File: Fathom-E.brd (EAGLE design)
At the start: 38.1 x 45.7 mm, 6 parts

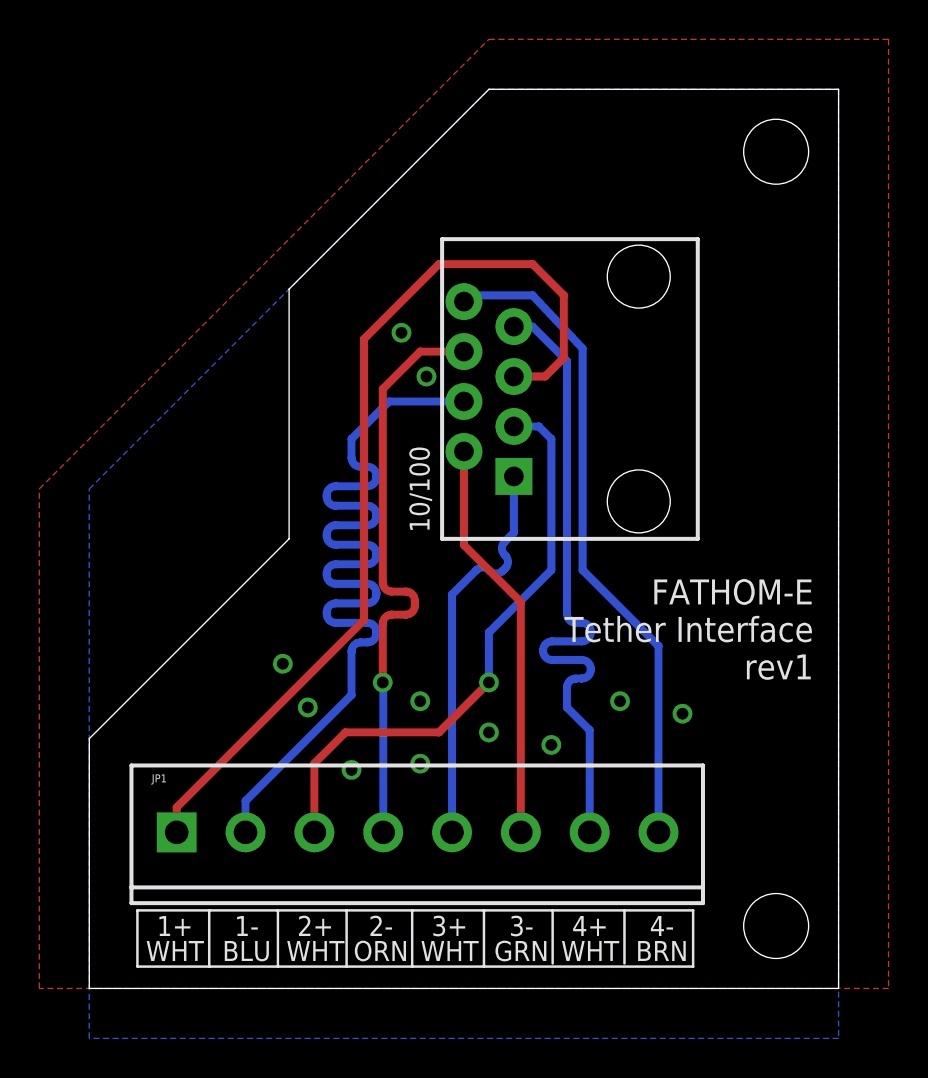
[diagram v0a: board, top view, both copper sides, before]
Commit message: Updated RJ45 position on Fathom-E
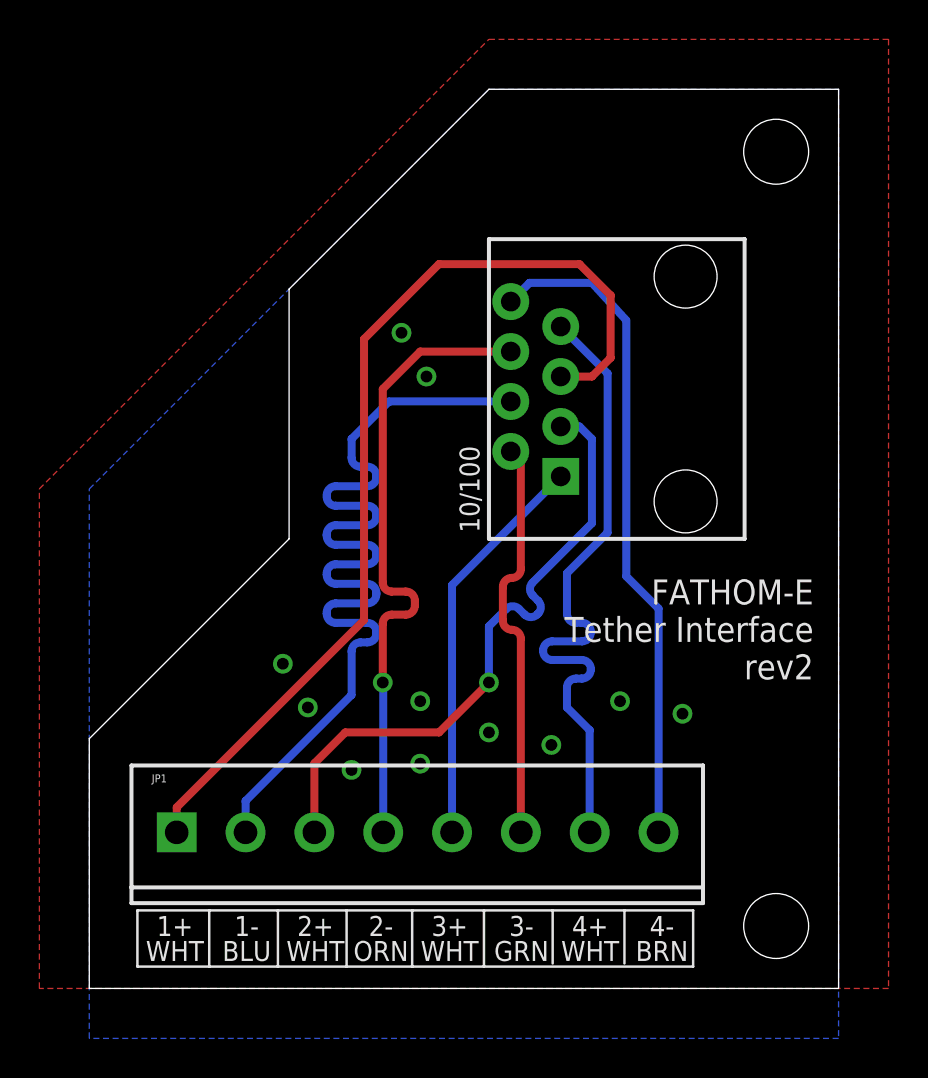
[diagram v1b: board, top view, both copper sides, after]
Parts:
- U$1: value RJ45-8PTH -> RJ45-8PTH-H; device SparkFun-Connectors:RJ45-8 -> BlueRobotics-Main:RJ45-8
- moved U$1 2.38 mm to (30.3, 30.5)
- moved U$7 1.27 mm to (30.8, 7.30)
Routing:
- net ORANGE: track 29.7 -> 32.0 mm
- net BLUE-WHITE: track 47.5 -> 49.9 mm
- net BLUE: track 46.1 -> 48.5 mm
- net ORANGE-WHITE: track 30.0 -> 32.0 mm
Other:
- board text added: "FATHOM-E Tether Interface rev2"
- board text added: "R.J. 2016/05"
- board text removed: "FATHOM-E Tether Interface rev1"
- board text removed: "R.J. 2016/02"
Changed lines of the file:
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@@
 <text x="36.83" y="18.25625" size="1.27" layer="21" ratio="12" align="center-right">FATHOM-E
 Tether Interface
-rev1</text>
+rev2</text>
 <wire x1="30.705" y1="3.96875" x2="27.2125" y2="3.96875" width="0.127" layer="21"/>
 <wire x1="27.2125" y1="3.96875" x2="23.56125" y2="3.96875" width="0.127" layer="21"/>
@@
 WHT</text>
 <text x="30.48" y="1.27" size="1.016" layer="22" rot="MR0">For cable lengths of 100m or less</text>
-<text x="10.16" y="19.84375" size="1.016" layer="22" ratio="12" rot="MR315">R.J. 2016/02</text>
-<text x="17.30375" y="23.1775" size="1.016" layer="21" ratio="12" rot="R90">10/100</text>
+<text x="10.16" y="19.84375" size="1.016" layer="22" ratio="12" rot="MR315">R.J. 2016/05</text>
+<text x="19.84375" y="23.1775" size="1.016" layer="21" ratio="12" rot="R90">10/100</text>
 </plain>
 <attributes>
@@
 <element name="STANDOFF3" library="SparkFun-Electromechanical" package="STAND-OFF" value="STAND-OFF" x="34.925" y="42.545"/>
 <element name="U$6" library="BlueRobotics-Main" package="BR-LOGO-MEDIUM-SMALL-COPPER" value="LOGOBR-LOGO-MS-COPPER" x="20.0025" y="39.37"/>
-<element name="U$7" library="BlueRobotics-Main" package="BR-FULL-LOGO-MEDIUM" value="LOGOFULL-M" x="29.5275" y="7.3025" rot="MR90"/>
-<element name="U$1" library="SparkFun-Connectors" package="RJ45-8" value="RJ45-8PTH" x="27.94" y="30.48" rot="R90"/>
+<element name="U$7" library="BlueRobotics-Main" package="BR-FULL-LOGO-MEDIUM" value="LOGOFULL-M" x="30.7975" y="7.3025" rot="MR90"/>
+<element name="U$1" library="BlueRobotics-Main" package="RJ45-8" value="RJ45-8PTH-H" x="30.32125" y="30.48" rot="R90"/>
 <element name="JP1" library="SparkFun-Connectors" package="SCREWTERMINAL-3.5MM-8" value="" x="4.445" y="7.9375"/>
 </elements>
@@
 <contactref element="U$1" pad="8"/>
 <contactref element="JP1" pad="8"/>
-<wire x1="28.945" y1="7.9375" x2="28.945" y2="17.41" width="0.4064" layer="16"/>
-<wire x1="28.945" y1="17.41" x2="25.0825" y2="21.2725" width="0.4064" layer="16"/>
-<wire x1="25.0825" y1="21.2725" x2="25.0825" y2="32.54375" width="0.4064" layer="16"/>
-<wire x1="25.0825" y1="32.54375" x2="22.5425" y2="35.2425" width="0.4064" layer="16"/>
-<wire x1="22.5425" y1="35.2425" x2="19.3675" y2="35.2425" width="0.4064" layer="16"/>
-<wire x1="19.3675" y1="35.2425" x2="19.05" y2="34.925" width="0.4064" layer="16"/>
+<wire x1="28.945" y1="7.9375" x2="28.945" y2="19.315" width="0.4064" layer="16"/>
+<wire x1="28.945" y1="19.315" x2="27.305" y2="20.955" width="0.4064" layer="16"/>
+<wire x1="27.305" y1="20.955" x2="27.305" y2="33.9725" width="0.4064" layer="16"/>
+<wire x1="27.305" y1="33.9725" x2="25.55875" y2="35.8775" width="0.4064" layer="16"/>
+<wire x1="25.55875" y1="35.8775" x2="22.38375" y2="35.8775" width="0.4064" layer="16"/>
+<wire x1="22.38375" y1="35.8775" x2="21.43125" y2="34.925" width="0.4064" layer="16"/>
 </signal>
 <signal name="BROWN-WHITE">
@@
 <wire x1="25.04365" y1="18.5928" x2="24.74595" y2="18.5928" width="0.4064" layer="16"/>
 <wire x1="24.74595" y1="18.5928" x2="24.28875" y2="19.05" width="0.4064" layer="16" curve="-90"/>
-<wire x1="24.28875" y1="19.05" x2="24.28875" y2="31.90875" width="0.4064" layer="16"/>
-<wire x1="24.28875" y1="31.90875" x2="22.5425" y2="33.655" width="0.4064" layer="16"/>
-<wire x1="22.5425" y1="33.655" x2="21.59" y2="33.655" width="0.4064" layer="16"/>
+<wire x1="24.28875" y1="19.05" x2="24.28875" y2="21.11375" width="0.4064" layer="16"/>
+<wire x1="24.28875" y1="21.11375" x2="26.3525" y2="23.1775" width="0.4064" layer="16"/>
+<wire x1="26.3525" y1="23.1775" x2="26.3525" y2="31.27375" width="0.4064" layer="16"/>
+<wire x1="26.3525" y1="31.27375" x2="23.97125" y2="33.655" width="0.4064" layer="16"/>
 </signal>
 <signal name="ORANGE">
@@
 <contactref element="JP1" pad="4"/>
 <wire x1="14.9225" y1="30.48" x2="16.8275" y2="32.385" width="0.4064" layer="1"/>
-<wire x1="16.8275" y1="32.385" x2="19.05" y2="32.385" width="0.4064" layer="1"/>
+<wire x1="16.8275" y1="32.385" x2="21.43125" y2="32.385" width="0.4064" layer="1"/>
 <wire x1="14.945" y1="7.9375" x2="14.945" y2="15.535" width="0.4064" layer="16"/>
 <wire x1="14.945" y1="15.535" x2="14.9225" y2="15.5575" width="0.4064" layer="16"/>
@@
 <wire x1="13.97" y1="18.7325" x2="13.97" y2="33.02" width="0.4064" layer="1"/>
 <wire x1="13.97" y1="33.02" x2="17.78" y2="36.83" width="0.4064" layer="1"/>
-<wire x1="17.78" y1="36.83" x2="22.5425" y2="36.83" width="0.4064" layer="1"/>
-<wire x1="22.5425" y1="36.83" x2="24.13" y2="35.2425" width="0.4064" layer="1"/>
-<wire x1="24.13" y1="35.2425" x2="24.13" y2="32.0675" width="0.4064" layer="1"/>
-<wire x1="24.13" y1="32.0675" x2="23.1775" y2="31.115" width="0.4064" layer="1"/>
-<wire x1="23.1775" y1="31.115" x2="21.59" y2="31.115" width="0.4064" layer="1"/>
+<wire x1="17.78" y1="36.83" x2="24.92375" y2="36.83" width="0.4064" layer="1"/>
+<wire x1="24.92375" y1="36.83" x2="26.51125" y2="35.2425" width="0.4064" layer="1"/>
+<wire x1="26.51125" y1="35.2425" x2="26.51125" y2="32.0675" width="0.4064" layer="1"/>
+<wire x1="26.51125" y1="32.0675" x2="25.55875" y2="31.115" width="0.4064" layer="1"/>
+<wire x1="25.55875" y1="31.115" x2="23.97125" y2="31.115" width="0.4064" layer="1"/>
 </signal>
 <signal name="BLUE">
@@
 <wire x1="13.335" y1="26.9875" x2="13.335" y2="27.94" width="0.4064" layer="16"/>
 <wire x1="13.335" y1="27.94" x2="15.24" y2="29.845" width="0.4064" layer="16"/>
-<wire x1="15.24" y1="29.845" x2="19.05" y2="29.845" width="0.4064" layer="16"/>
+<wire x1="15.24" y1="29.845" x2="21.43125" y2="29.845" width="0.4064" layer="16"/>
 </signal>
 <signal name="ORANGE-WHITE">
@@
 <wire x1="17.78" y1="13.0175" x2="20.32" y2="15.5575" width="0.4064" layer="1"/>
 <via x="20.32" y="15.5575" extent="1-16" drill="0.6"/>
-<wire x1="20.32" y1="15.5575" x2="20.32" y2="18.0975" width="0.4064" layer="16"/>
-<wire x1="20.32" y1="18.0975" x2="23.495" y2="21.2725" width="0.4064" layer="16"/>
-<wire x1="23.495" y1="21.2725" x2="23.495" y2="27.94" width="0.4064" layer="16"/>
-<wire x1="23.495" y1="27.94" x2="22.86" y2="28.575" width="0.4064" layer="16"/>
-<wire x1="22.86" y1="28.575" x2="21.59" y2="28.575" width="0.4064" layer="16"/>
+<wire x1="20.32" y1="15.5575" x2="20.32" y2="18.415" width="0.4064" layer="16"/>
+<wire x1="20.32" y1="18.415" x2="21.202959375" y2="19.297959375" width="0.4064" layer="16"/>
+<wire x1="21.202959375" y1="19.297959375" x2="21.8495375" y2="19.297959375" width="0.4064" layer="16" curve="-90"/>
+<wire x1="21.8495375" y1="19.297959375" x2="22.1313875" y2="19.016109375" width="0.4064" layer="16"/>
+<wire x1="22.1313875" y1="19.016109375" x2="22.777965625" y2="19.016109375" width="0.4064" layer="16" curve="90"/>
+<wire x1="22.777965625" y1="19.016109375" x2="22.82435" y2="19.06249375" width="0.4064" layer="16"/>
+<wire x1="22.82435" y1="19.06249375" x2="22.82435" y2="19.709071875" width="0.4064" layer="16" curve="90"/>
+<wire x1="22.82435" y1="19.709071875" x2="22.5425" y2="19.990921875" width="0.4064" layer="16"/>
+<wire x1="22.5425" y1="19.990921875" x2="22.5425" y2="20.6375" width="0.4064" layer="16" curve="-90"/>
+<wire x1="22.5425" y1="20.6375" x2="25.55875" y2="23.65375" width="0.4064" layer="16"/>
+<wire x1="25.55875" y1="23.65375" x2="25.55875" y2="27.94" width="0.4064" layer="16"/>
+<wire x1="25.55875" y1="27.94" x2="24.92375" y2="28.575" width="0.4064" layer="16"/>
+<wire x1="24.92375" y1="28.575" x2="23.97125" y2="28.575" width="0.4064" layer="16"/>
 </signal>
 <signal name="GREEN">
 <contactref element="U$1" pad="2"/>
 <contactref element="JP1" pad="6"/>
-<wire x1="21.945" y1="7.9375" x2="21.945" y2="19.6475" width="0.4064" layer="1"/>
-<wire x1="21.945" y1="19.6475" x2="19.05" y2="22.5425" width="0.4064" layer="1"/>
-<wire x1="19.05" y1="22.5425" x2="19.05" y2="27.305" width="0.4064" layer="1"/>
+<wire x1="21.945" y1="26.79125" x2="21.945" y2="21.33311875" width="0.4064" layer="1"/>
+<wire x1="21.945" y1="21.33311875" x2="21.4878" y2="20.87591875" width="0.4064" layer="1" curve="-90"/>
+<wire x1="21.4878" y1="20.87591875" x2="21.0306" y2="20.41871875" width="0.4064" layer="1" curve="90"/>
+<wire x1="21.0306" y1="20.41871875" x2="21.0306" y2="18.6944" width="0.4064" layer="1"/>
+<wire x1="21.0306" y1="18.6944" x2="21.4878" y2="18.2372" width="0.4064" layer="1" curve="90"/>
+<wire x1="21.4878" y1="18.2372" x2="21.945" y2="17.78" width="0.4064" layer="1" curve="-90"/>
+<wire x1="21.945" y1="17.78" x2="21.945" y2="7.9375" width="0.4064" layer="1"/>
+<wire x1="21.945" y1="26.79125" x2="21.43125" y2="27.305" width="0.4064" layer="1"/>
 </signal>
 <signal name="GREEN-WHITE">
 <contactref element="U$1" pad="1"/>
 <contactref element="JP1" pad="5"/>
-<wire x1="18.445" y1="7.9375" x2="18.445" y2="20.0325" width="0.4064" layer="16"/>
-<wire x1="21.59" y1="23.1775" x2="21.11381875" y2="22.70131875" width="0.4064" layer="16"/>
-<wire x1="21.11381875" y1="22.70131875" x2="21.11381875" y2="22.054740625" width="0.4064" layer="16" curve="90"/>
-<wire x1="21.11381875" y1="22.054740625" x2="21.156571875" y2="22.0119875" width="0.4064" layer="16"/>
-<wire x1="21.156571875" y1="22.0119875" x2="21.156571875" y2="21.36540625" width="0.4064" layer="16" curve="-90"/>
-<wire x1="21.156571875" y1="21.36540625" x2="21.0209125" y2="21.229746875" width="0.4064" layer="16"/>
-<wire x1="21.0209125" y1="21.229746875" x2="20.37433125" y2="21.229746875" width="0.4064" layer="16" curve="-90"/>
-<wire x1="20.37433125" y1="21.229746875" x2="20.331578125" y2="21.2725" width="0.4064" layer="16"/>
-<wire x1="20.331578125" y1="21.2725" x2="19.685" y2="21.2725" width="0.4064" layer="16" curve="90"/>
-<wire x1="19.685" y1="21.2725" x2="18.445" y2="20.0325" width="0.4064" layer="16"/>
-<wire x1="21.59" y1="23.1775" x2="21.59" y2="26.035" width="0.4064" layer="16"/>
+<wire x1="18.445" y1="7.9375" x2="18.445" y2="20.50875" width="0.4064" layer="16"/>
+<wire x1="18.445" y1="20.50875" x2="23.97125" y2="26.035" width="0.4064" layer="16"/>
 </signal>
 </signals>
